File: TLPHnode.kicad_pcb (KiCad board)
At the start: 2 copper layers, 0 parts

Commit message: Check-point
  - some parts tentatively placed
  - commiting before adding any traces
  - design rules set. OSH 4-layer
On branch master
modified:   TLPHnode-cache.lib
modified:   TLPHnode.kicad_pcb
new file:   TLPHnode.net
modified:   TLPHnode.sch
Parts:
- added C1: 1 uF, Capacitors_SMD:C_0603, F.Cu at (156.2, 77.0)
- added C2: 0.1 uF, Capacitors_SMD:C_0603, F.Cu at (182.1, 79.4)
- added C3: 1 uF, Capacitors_SMD:C_0603, F.Cu at (155.7, 71.5)
- added C4: 0.1 uF, Capacitors_SMD:C_0603, F.Cu at (177.7, 85.2)
- added C5: 0.1 uF, Capacitors_SMD:C_0603, F.Cu at (172.2, 91.0)
- added C6: 0.1 uF, Capacitors_SMD:C_0603, F.Cu at (162.8, 102.0)
- added P1: Bat, rockingdlabs:JST_PH_S2B-PH-SM4-TB_02x2.00mm_Angled, F.Cu at (156.7, 83.5)
- added P2: CONN_01X05, rockingdlabs:FPC_conn-5_8x4.9mm_Pitch0.5mm, F.Cu at (154.5, 95.8)
- added R1: 4.7k, Resistors_SMD:R_0603, F.Cu at (164.7, 95.7)
- added R10: 4.7k, Resistors_SMD:R_0603, F.Cu at (174.9, 96.9)
- added R11: 4.7k, Resistors_SMD:R_0603, F.Cu at (171.1, 102.7)
- added R12: 4.7k, Resistors_SMD:R_0603, F.Cu at (184.3, 91.1)
- added R13: 4.7k, Resistors_SMD:R_0603, F.Cu at (178.7, 96.9)
- added R14: 4.7k, Resistors_SMD:R_0603, F.Cu at (189.6, 85.2)
- added R2: 4.7k, Resistors_SMD:R_0603, F.Cu at (171.4, 85.1)
- added R3: 4.7k, Resistors_SMD:R_0603, F.Cu at (177.5, 79.4)
- added R4: 4.7k, Resistors_SMD:R_0603, F.Cu at (176.8, 91.1)
- added R5: 10k, Resistors_SMD:R_0603, F.Cu at (168.2, 96.8)
- added R6: 10k, Resistors_SMD:R_0603, F.Cu at (171.4, 96.8)
- added R7: 10k, Resistors_SMD:R_0603, F.Cu at (182.0, 85.2)
- added R8: 4.7k, Resistors_SMD:R_0603, F.Cu at (167.4, 102.7)
- added R9: 4.7k, Resistors_SMD:R_0603, F.Cu at (180.6, 91.1)
- added SW1: Reset, rockingdlabs:ESwitch-SMD-4, F.Cu at (164.6, 82.8)
- added U1: NCP703, rockingdlabs:NCP703-TSOP-5, F.Cu at (156.6, 74.2)
- added U2: LD39130S, rockingdlabs:LD39130S-FlipChip-4, F.Cu at (156.6, 74.2)
- added U3: LPS25HB, rockingdlabs:LPS25HB-HLGA-10L-2.5x2.5mm, F.Cu at (142.6, 86.4)
- added U4: Si7006-A20, rockingdlabs:Si7006_A20-DFN-6, F.Cu at (142.5, 90.0)
- added U5: ESP-12E, ESP8266:ESP-12E, B.Cu at (131.8, 83.8)
- added U6: ISL29035, rockingdlabs:ISL29035-DFN-6-1.5x1.6mm_Pitch0.5mm, F.Cu at (138.3, 89.3)
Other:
- copper layers 2 -> 4
- net class 2layerMin added: clearance 0.1524, trace_width 0.1524, via_dia 0.6858, via_drill 0.3302
- net class 4layerMin added: clearance 0.127, trace_width 0.127, via_dia 0.4572, via_drill 0.254
- net class Default: clearance 0.2 -> 0.14478; trace_width 0.25 -> 0.14478; via_dia 0.8 -> 0.508; via_drill 0.4 -> 0.254
- rule trace_clearance: 0.2 -> 0.14478
- rule trace_min: 0.2 -> 0.127
- rule via_min_drill: 0.3 -> 0.254
- rule via_min_size: 0.4 -> 0.4572

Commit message: Check-point: First placement
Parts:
- P1, SW1: moved to B.Cu
- moved R14 51.1 mm to (139.6, 95.8), turned to 270 degrees
- moved R12 46.7 mm to (137.9, 95.9), turned to 270 degrees
- moved R9 45.0 mm to (135.8, 95.7), turned to 270 degrees
- moved R13 44.4 mm to (134.4, 93.2), turned to 90 degrees
- moved R4 41.4 mm to (135.8, 85.9), turned to 90 degrees
- moved R7 40.3 mm to (141.8, 85.8), turned to 270 degrees
- moved R3 38.8 mm to (141.2, 93.2), turned to 90 degrees
- moved C2 35.9 mm to (147.6, 89.0)
- moved R2 34.4 mm to (137.9, 93.2), turned to 90 degrees
- moved C6 33.1 mm to (131.8, 90.4), turned to 270 degrees
- moved R10 32.9 mm to (143.5, 87.1), turned to 270 degrees
- moved C5 29.2 mm to (143.1, 90.5), turned to 270 degrees
- moved R6 28.5 mm to (145.2, 85.7), turned to 270 degrees
- moved R11 28.2 mm to (143.8, 95.6), turned to 90 degrees
- moved C4 27.7 mm to (151.0, 92.5), turned to 90 degrees
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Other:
- board outline added: 29 x 20.5 mm

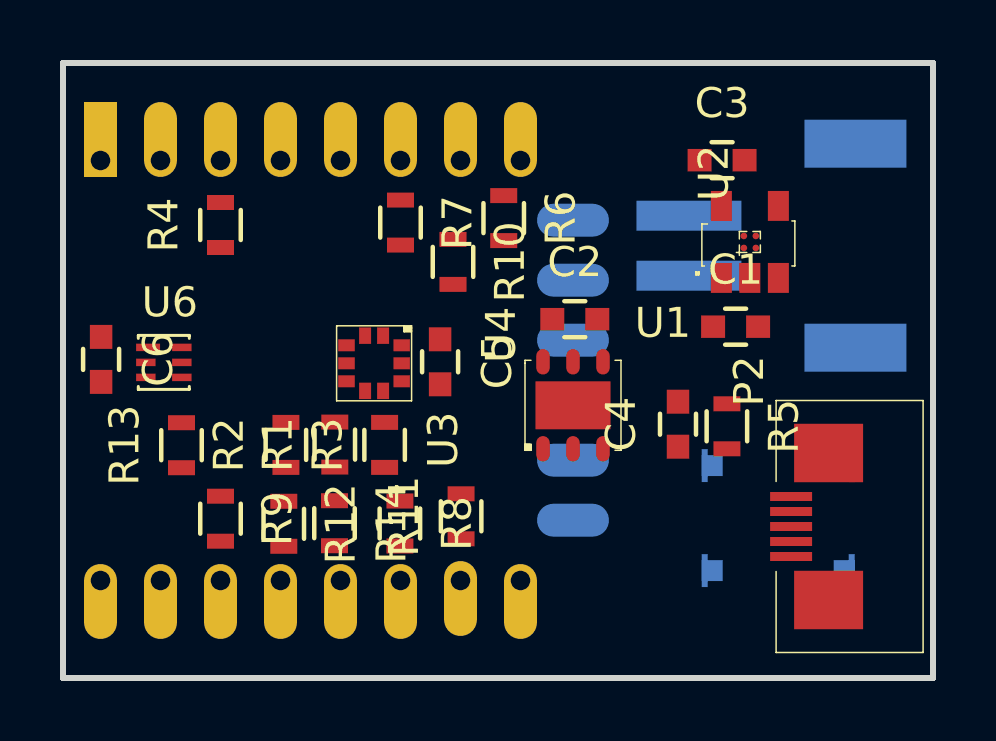
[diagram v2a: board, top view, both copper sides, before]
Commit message: Check-point: 28x20.5mm board
    - Only ESP-12E and power connector on the back
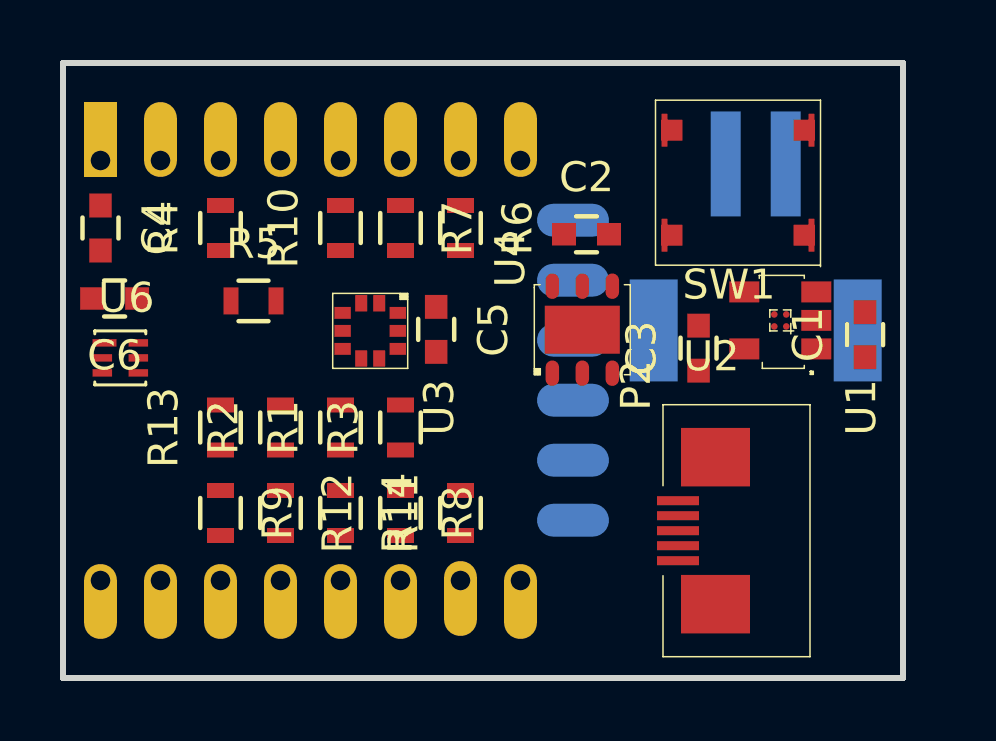
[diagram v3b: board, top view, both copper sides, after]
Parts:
- SW1: moved to F.Cu
- moved C4 20.3 mm to (131.8, 86.0), turned to 270 degrees
- moved R5 16.3 mm to (136.8, 88.4), turned to 0 degrees
- moved SW1 11.3 mm to (153.0, 84.5), turned to 180 degrees
- moved C3 6.31 mm to (151.7, 90.0), turned to 90 degrees
- moved C1 4.32 mm to (157.2, 89.6), turned to 90 degrees
- moved R10 3.92 mm to (139.8, 86.0), turned to 90 degrees
- moved P2 3.77 mm to (152.8, 96.1)
- moved C2 2.86 mm to (147.9, 86.2)
- moved U1 2.81 mm to (154.4, 89.1), turned to 270 degrees
- moved U2 2.81 mm to (154.4, 89.1), turned to 180 degrees
- moved U4 2.54 mm to (147.8, 89.4)
- moved C6 2.08 mm to (132.2, 88.3), turned to 180 degrees
- moved R6 1.48 mm to (143.8, 86.0)
- moved U6 1.46 mm to (132.4, 90.3)
- moved R13 1.43 mm to (135.8, 92.7)
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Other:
- board size 29 x 20.5 mm -> 28 x 20.5 mm

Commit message: Check-point: layout passes DRM, References visible
On branch master
modified:   TLPHnode-cache.lib
modified:   TLPHnode.kicad_pcb
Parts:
- moved R5 2.59 mm to (137.8, 86.0), turned to 90 degrees
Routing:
- net VCC: track 0.00 -> 42.1 mm, vias 0 -> 11
- net Net-(C4-Pad1): track 0.00 -> 32.4 mm
- net GND: track 0.00 -> 31.7 mm, vias 0 -> 9
- net /I2C_SDA: track 0.00 -> 25.1 mm, vias 0 -> 3
- net /TXD: track 0.00 -> 22.7 mm
- net /I2C_SCL: track 0.00 -> 21.2 mm
- net /RXD: track 0.00 -> 20.4 mm
- net /PGM: track 0.00 -> 13.3 mm
- net Net-(C1-Pad1): track 0.00 -> 10.3 mm, vias 0 -> 1
- net Net-(R13-Pad2): track 0.00 -> 3.41 mm
- net Net-(R2-Pad2): track 0.00 -> 2.84 mm
- net Net-(R3-Pad2): track 0.00 -> 1.96 mm
- net Net-(R1-Pad2): track 0.00 -> 1.95 mm
- net Net-(R9-Pad2): track 0.00 -> 1.50 mm
- net Net-(R7-Pad1): track 0.00 -> 1.50 mm
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- added copper zone on In1.Cu.GND, net GND
- added copper zone on In2.Cu.VCC, net VCC

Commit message: Add copyright notice, partname and date
On branch master
modified:   TLPHnode.kicad_pcb
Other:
- board text added: "Copyright 2016 J. Dunmire, All Rights Reserved"
- board text added: "TLPHnode 2016/12/09"
- board text added: "jerry@dunmire.org"
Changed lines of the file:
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@@
     (links 78)
     (no_connects 0)
-    (area 122.822599 79.7301 160.1799 101.100001)
+    (area 130.399999 80.399999 158.600001 101.100001)
     (thickness 1.6)
-    (drawings 4)
+    (drawings 7)
     (tracks 221)
     (zones 0)
@@
   (layers
     (0 F.Cu signal)
-    (1 In1.Cu.GND power hide)
-    (2 In2.Cu.VCC power hide)
-    (31 B.Cu signal hide)
+    (1 In1.Cu.GND power)
+    (2 In2.Cu.VCC power)
+    (31 B.Cu signal)
     (32 B.Adhes user)
     (33 F.Adhes user)
@@
     (aux_axis_origin 0 0)
     (grid_origin 147.74 99.99)
-    (visible_elements FFFEFB7F)
+    (visible_elements FFFEFF7F)
     (pcbplotparams
       (layerselection 0x00030_ffffffff)
@@
   (module rockingdlabs:NCP703-TSOP-5 (layer F.Cu)
     (at 154.41 89.08 270)
-    (fp_text reference U1 (at 2.9 -2.7 270) (layer F.SilkS)
+    (fp_text reference U1 (at 2.21 -1.23 360) (layer F.SilkS)
       (effects (font (size 1 1) (thickness 0.15)))
     )
@@
   (module rockingdlabs:LD39130S-FlipChip-4 (layer F.Cu)
     (at 154.41 89.08 180)
-    (fp_text reference U2 (at 0.87 2.19 180) (layer F.SilkS)
-      (effects (font (size 1 1) (thickness 0.15)))
+    (fp_text reference U2 (at 1.17 -0.01 180) (layer F.SilkS)
+      (effects (font (size 0.5 0.5) (thickness 0.1)))
     )
     (fp_text value LD39130S (at 0.25 -4.25 180) (layer F.Fab)
@@
   (module rockingdlabs:LPS25HB-HLGA-10L-2.5x2.5mm (layer F.Cu)
     (at 140.74 89.43 270)
-    (fp_text reference U3 (at 1.56 2.2 360) (layer F.SilkS)
+    (fp_text reference U3 (at 1.56 2.2) (layer F.SilkS)
       (effects (font (size 1 1) (thickness 0.15)))
     )
@@
     )
   )
+  (gr_text jerry@dunmire.org (at 144.54 81.29 180) (layer F.SilkS)
+    (effects (font (size 0.5 0.5) (thickness 0.1)))
+  )
+  (gr_text "Copyright 2016 J. Dunmire, All Rights Reserved" (at 141.24 100.09) (layer F.SilkS)
+    (effects (font (size 0.5 0.5) (thickness 0.1)))
+  )
+  (gr_text "TLPHnode\n2016/12/09" (at 156.94 97.69 90) (layer F.SilkS)
+    (effects (font (size 0.5 0.5) (thickness 0.1)))
+  )
   (gr_line (start 158.5 80.5) (end 130.5 80.5) (angle 90) (layer Edge.Cuts) (width 0.2))

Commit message: Add Logo
On branch master
modified:   TLPHnode.kicad_pcb
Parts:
- added Ref**: RockingDLogo_9x7, rockingDLogos:RockingDLogo_9x7, B.Cu at (157.8, 96.0)
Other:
- board text added: "GND"
- board text added: "VBat"
- board text added: "VCC"

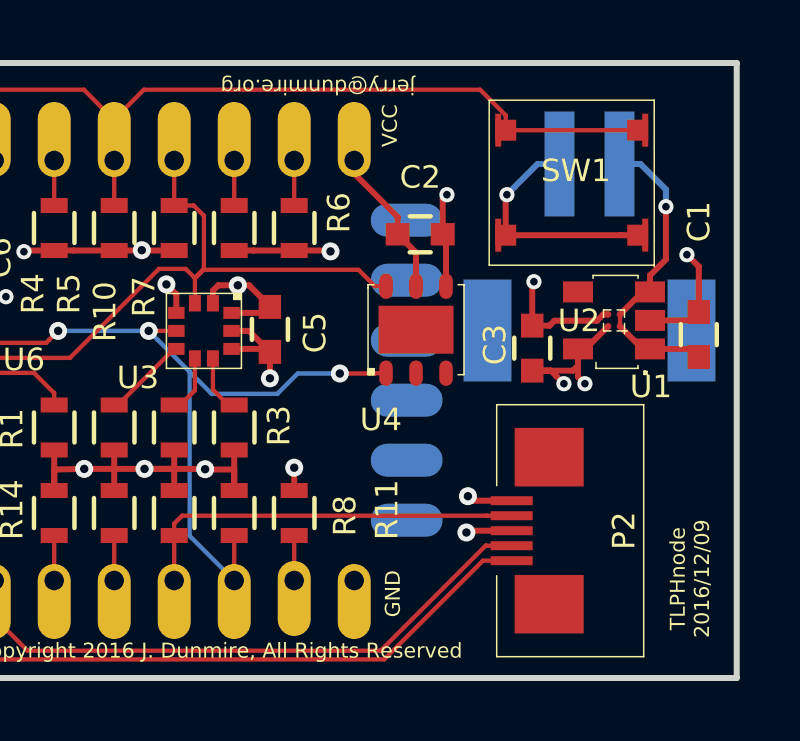
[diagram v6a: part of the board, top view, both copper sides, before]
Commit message: Change Bat to a through-hole connector
  - Add VBat to P2 so that a single connector can
    be used when connecting to a charger/breakout/debug board
  - Use a two-pin through-hole header for VBat to make it
    easy to solder wires rather than use a connector.

On branch AltPower
modified:   TLPHnode-cache.lib
modified:   TLPHnode.kicad_pcb
modified:   TLPHnode.net
modified:   TLPHnode.sch
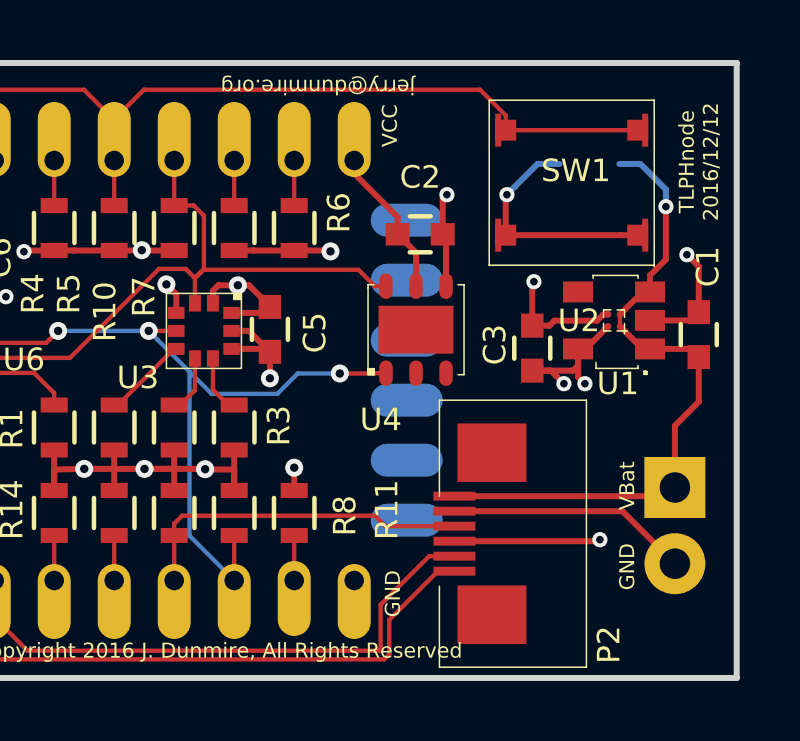
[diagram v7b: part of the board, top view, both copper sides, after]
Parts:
- P1: footprint rockingdlabs:JST_PH_S2B-PH-SM4-TB_02x2.00mm_Angled -> Socket_Strips:Socket_Strip_Straight_1x02
- P2: value CONN_01X05 -> CONN_01X06; footprint rockingdlabs:FPC_conn-5_8x4.9mm_Pitch0.5mm -> rockingdlabs:FPC_conn-6_8x4.9mm_Pitch0.5mm
- moved Ref** 9.81 mm to (157.4, 86.2)
- moved P1 8.50 mm to (156.4, 94.7), turned to 270 degrees
- moved P2 1.91 mm to (150.8, 96.2)
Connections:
- C1 pad 1: Net-(C1-Pad1) -> /VBat
- P1 pad 1: Net-(C1-Pad1) -> /VBat
- U1 pad 1: Net-(C1-Pad1) -> /VBat
- U1 pad 3: Net-(C1-Pad1) -> /VBat
- U2 pad A1: Net-(C1-Pad1) -> /VBat
- U2 pad B1: Net-(C1-Pad1) -> /VBat
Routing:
- net /VBat: track 0.00 -> 22.4 mm, vias 0 -> 1
- net Net-(C1-Pad1): track 10.3 -> 0.00 mm, vias 1 -> 0
- net GND: track 31.7 -> 38.2 mm, vias 9 -> 8
- net VCC: track 42.1 -> 45.4 mm
- net /PGM: track 13.3 -> 11.5 mm
- net /TXD: track 22.7 -> 21.3 mm
- net /RXD: track 20.4 -> 19.2 mm
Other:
- board text added: "TLPHnode 2016/12/12"
- board text removed: "TLPHnode 2016/12/09"

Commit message: Change battery connection to bare pads
    - Use pin model rather than socket
    - remove 3d model
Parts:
- P1: footprint Socket_Strips:Socket_Strip_Straight_1x02 -> Pin_Headers:Pin_Header_Straight_1x02
- turned P1 to 180 degrees
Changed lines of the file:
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@@
   )
   (setup
-    (last_trace_width 0.2)
+    (last_trace_width 0.14478)
     (user_trace_width 0.15)
     (user_trace_width 0.175)
@@
     (diff_pair_width 0.127)
   )
-  (module Socket_Strips:Socket_Strip_Straight_1x02 (layer B.Cu)
-    (at 156.44 94.65 270)
-    (descr "Through hole socket strip")
-    (tags "socket strip")
-    (fp_text reference P1 (at -2.66 0.7 270) (layer B.SilkS)
+  (module Pin_Headers:Pin_Header_Straight_1x02 (layer B.Cu)
+    (at 156.44 94.65 180)
+    (descr "Through hole pin header")
+    (tags "pin header")
+    (fp_text reference P1 (at 0 5.1 180) (layer B.SilkS)
       (effects (font (size 1 1) (thickness 0.15)) (justify mirror))
     )
-    (fp_text value Bat (at 0 3.1 270) (layer B.Fab)
+    (fp_text value Bat (at 0 3.1 180) (layer B.Fab)
       (effects (font (size 1 1) (thickness 0.15)) (justify mirror))
     )
-    (fp_line (start -1.55 -1.55) (end 0 -1.55) (layer B.SilkS) (width 0.15))
-    (fp_line (start 3.81 -1.27) (end 1.27 -1.27) (layer B.SilkS) (width 0.15))
-    (fp_line (start -1.75 1.75) (end -1.75 -1.75) (layer B.CrtYd) (width 0.05))
-    (fp_line (start 4.3 1.75) (end 4.3 -1.75) (layer B.CrtYd) (width 0.05))
-    (fp_line (start -1.75 1.75) (end 4.3 1.75) (layer B.CrtYd) (width 0.05))
-    (fp_line (start -1.75 -1.75) (end 4.3 -1.75) (layer B.CrtYd) (width 0.05))
-    (fp_line (start 1.27 -1.27) (end 1.27 1.27) (layer B.SilkS) (width 0.15))
-    (fp_line (start 0 1.55) (end -1.55 1.55) (layer B.SilkS) (width 0.15))
-    (fp_line (start -1.55 1.55) (end -1.55 -1.55) (layer B.SilkS) (width 0.15))
-    (fp_line (start 1.27 1.27) (end 3.81 1.27) (layer B.SilkS) (width 0.15))
-    (fp_line (start 3.81 1.27) (end 3.81 -1.27) (layer B.SilkS) (width 0.15))
-    (pad 1 thru_hole rect (at 0 0 270) (size 2.032 2.032) (drill 1.016) (layers *.Cu *.Mask)
+    (fp_line (start 1.27 -1.27) (end 1.27 -3.81) (layer B.SilkS) (width 0.15))
+    (fp_line (start 1.55 1.55) (end 1.55 0) (layer B.SilkS) (width 0.15))
+    (fp_line (start -1.75 1.75) (end -1.75 -4.3) (layer B.CrtYd) (width 0.05))
+    (fp_line (start 1.75 1.75) (end 1.75 -4.3) (layer B.CrtYd) (width 0.05))
+    (fp_line (start -1.75 1.75) (end 1.75 1.75) (layer B.CrtYd) (width 0.05))
+    (fp_line (start -1.75 -4.3) (end 1.75 -4.3) (layer B.CrtYd) (width 0.05))
+    (fp_line (start 1.27 -1.27) (end -1.27 -1.27) (layer B.SilkS) (width 0.15))
+    (fp_line (start -1.55 0) (end -1.55 1.55) (layer B.SilkS) (width 0.15))
+    (fp_line (start -1.55 1.55) (end 1.55 1.55) (layer B.SilkS) (width 0.15))
+    (fp_line (start -1.27 -1.27) (end -1.27 -3.81) (layer B.SilkS) (width 0.15))
+    (fp_line (start -1.27 -3.81) (end 1.27 -3.81) (layer B.SilkS) (width 0.15))
+    (pad 1 thru_hole rect (at 0 0 180) (size 2.032 2.032) (drill 1.016) (layers *.Cu *.Mask)
       (net 28 /VBat))
-    (pad 2 thru_hole oval (at 2.54 0 270) (size 2.032 2.032) (drill 1.016) (layers *.Cu *.Mask)
-      (net 1 GND))
-    (model Socket_Strips.3dshapes/Socket_Strip_Straight_1x02.wrl
-      (at (xyz 0.05 0 0))
-      (scale (xyz 1 1 1))
-      (rotate (xyz 0 0 180))
-    )
+    (pad 2 thru_hole oval (at 0 -2.54 180) (size 2.032 2.032) (drill 1.016) (layers *.Cu *.Mask)
+      (net 1 GND))
   )
   (module rockingdlabs:FPC_conn-6_8x4.9mm_Pitch0.5mm (layer F.Cu)
@@
   (segment (start 135.07478 90.83) (end 135.75 91.50522) (width 0.14478) (layer F.Cu) (net 18))
   (segment (start 135.75 91.50522) (end 135.75 91.9) (width 0.14478) (layer F.Cu) (net 18))
-  (segment (start 149.09 94.94) (end 156.15 94.94) (width 0.2) (layer F.Cu) (net 28))
-  (segment (start 156.15 94.94) (end 156.44 94.65) (width 0.2) (layer F.Cu) (net 28))
   (segment (start 156.44 92.59) (end 157.235 91.795) (width 0.2) (layer F.Cu) (net 28))
   (segment (start 157.235 91.795) (end 157.235 90.305) (width 0.2) (layer F.Cu) (net 28))
   (segment (start 156.44 94.65) (end 156.44 92.59) (width 0.2) (layer F.Cu) (net 28))
+  (segment (start 149.09 94.94) (end 156.15 94.94) (width 0.2) (layer F.Cu) (net 28))
+  (segment (start 156.15 94.94) (end 156.44 94.65) (width 0.2) (layer F.Cu) (net 28))
   (segment (start 154.59 83.865) (end 155.29 83.865) (width 0.2) (layer B.Cu) (net 28))
   (segment (start 155.29 83.865) (end 156.140006 84.715006) (width 0.2) (layer B.Cu) (net 28))
